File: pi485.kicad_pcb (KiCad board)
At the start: 2 copper layers, 70 x 48 mm, 29 parts, among them J1 RS485, P1 Rasperry Pi, P2 PWR, P3 Term, P4 Latch Disable, Q1 2N4401, Q2 2N4401, U1 NE555, U2 MAX485

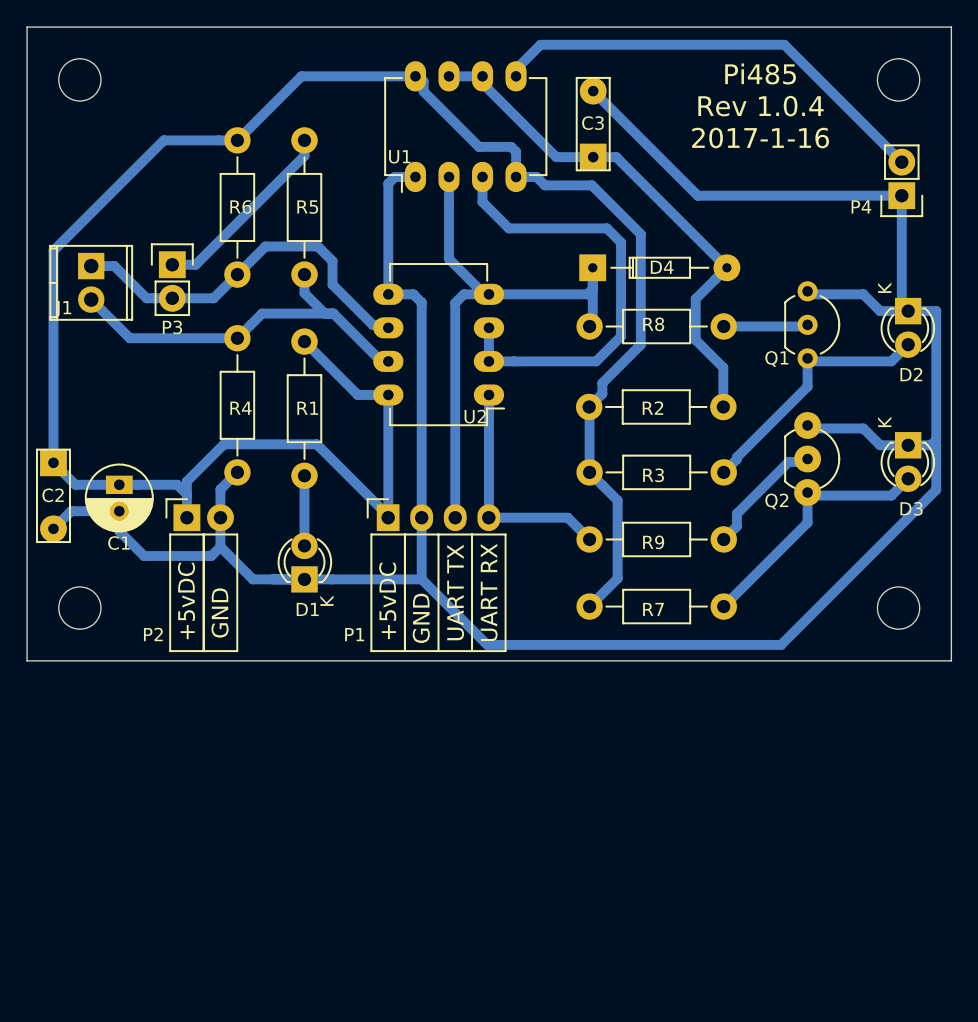
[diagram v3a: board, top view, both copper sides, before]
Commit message: 1.1.0 bump. Added 3.3v control pin to turn on power to the 485 and the PWR LED.
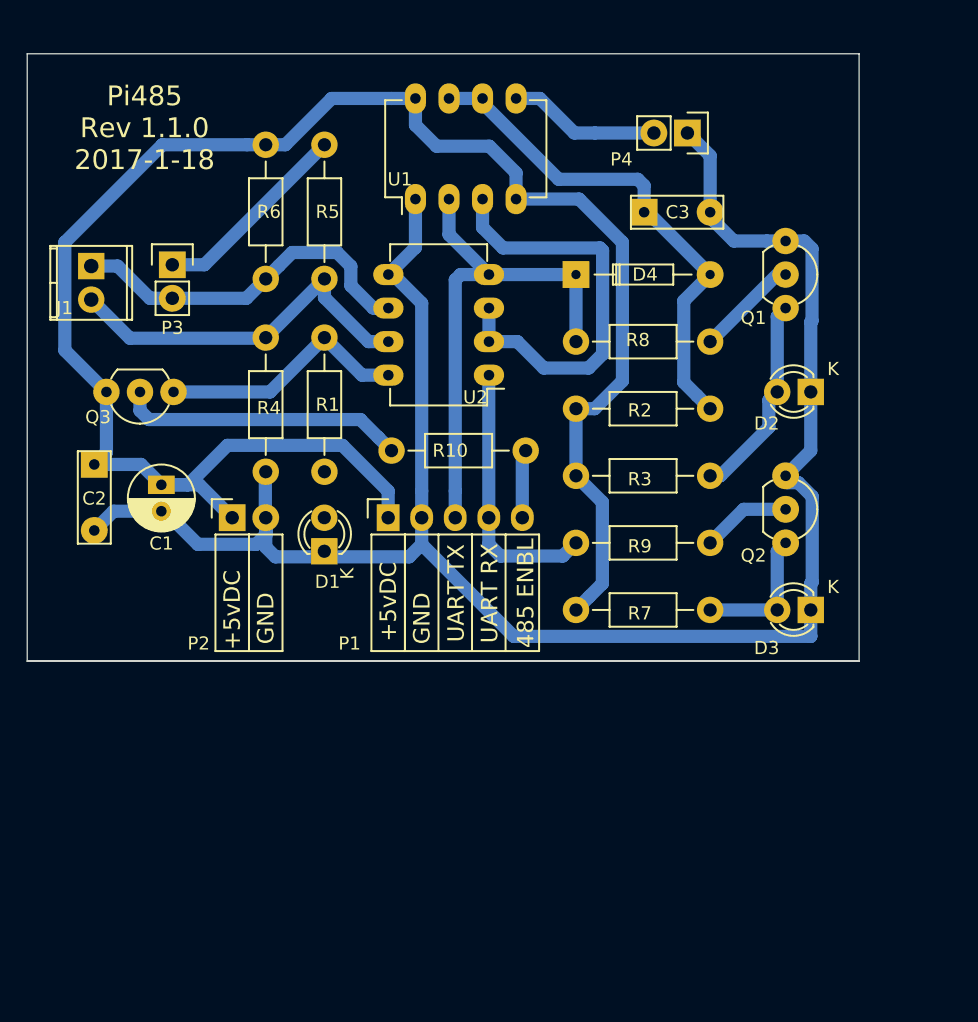
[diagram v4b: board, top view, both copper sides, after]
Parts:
- removed REF01, REF02, REF03, REF04: MountingHole_3.2mm_M3, Mounting_Holes:MountingHole_3.2mm_M3
- added Q3: 2N4401, TO_SOT_Packages_THT:TO-92_Inline_Wide, F.Cu at (23.4, 40.0)
- added R10: 270, Resistors_THT:Resistor_Horizontal_RM10mm, F.Cu at (39.9, 44.4)
- P1: footprint Socket_Strips:Socket_Strip_Angled_1x04 -> Socket_Strips:Socket_Strip_Angled_1x05
- R1: value 120 -> 200
- moved P4 16.9 mm to (62.3, 20.3), turned to 270 degrees
- moved D3 14.5 mm to (71.7, 56.5), turned to 180 degrees
- moved D2 9.59 mm to (71.7, 40.0), turned to 180 degrees
- moved C3 5.68 mm to (59.1, 26.3), turned to 0 degrees
- moved Q1 4.16 mm to (69.8, 28.5)
- moved Q2 4.16 mm to (69.8, 46.3)
- moved P2 3.43 mm to (27.9, 49.5)
- moved C1 3.19 mm to (22.5, 47.0)
- moved C2 3.09 mm to (17.4, 45.4)
- moved D1 2.61 mm to (34.8, 52.0)
- moved R6 2.17 mm to (30.4, 31.4)
- moved R4 2.15 mm to (30.4, 46.0)
- moved U1 1.68 mm to (41.7, 25.3)
- moved R5 1.55 mm to (34.9, 31.4)
- moved R1 1.54 mm to (34.9, 35.8)
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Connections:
- R1 pad 1: VCC -> Net-(Q3-Pad3)
- U2 pad 8: VCC -> Net-(Q3-Pad3)
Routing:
- net GND: track 192.4 -> 143.7 mm
- net Net-(P4-Pad2): track 34.2 -> 11.5 mm
- net Net-(Q3-Pad2): track 0.00 -> 21.7 mm
- net Net-(Q3-Pad3): track 0.00 -> 19.2 mm
- net VCC: track 154.5 -> 137.9 mm
- net Net-(D3-Pad2): track 19.2 -> 10.4 mm
- net Net-(D1-Pad2): track 5.56 -> 0.00 mm
- net /(485PWR)_GPIO18: track 0.00 -> 5.19 mm
- net /(TXDO)_GPIO14: track 43.9 -> 39.4 mm
- net Net-(D2-Pad2): track 19.2 -> 15.5 mm
- net Net-(U1-Pad3): track 35.2 -> 32.2 mm
- net Net-(Q2-Pad2): track 9.97 -> 7.13 mm
- net /(RXDO)_GPIO15: track 17.6 -> 20.2 mm
- net Net-(J1-Pad2): track 30.2 -> 28.3 mm
- net Net-(C3-Pad1): track 39.7 -> 38.5 mm
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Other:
- board size 70 x 48 mm -> 63 x 46 mm
- net class Default: clearance 0.75 -> 0.5; trace_width 0.75 -> 1
- rule trace_clearance: 0.75 -> 0.5
- rule trace_min: 0.75 -> 1
- board text added: "485 ENBL"
- board text added: "Pi485 Rev 1.1.0 2017-1-18"
- board text removed: "Pi485 Rev 1.0.4 2017-1-16"

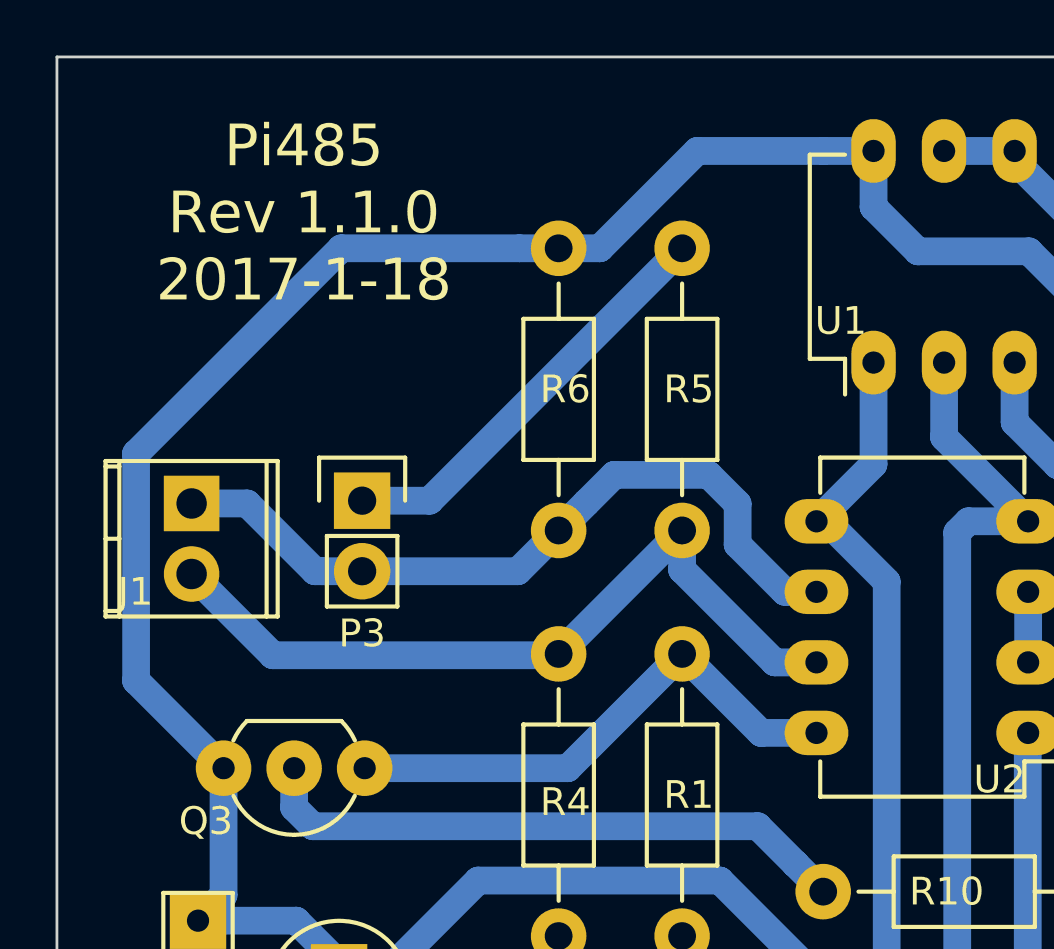
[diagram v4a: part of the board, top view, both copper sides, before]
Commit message: VCC control of the 555. Using a GPIO pin, we can reduce overall power consumption by turning things off when we don't need them.
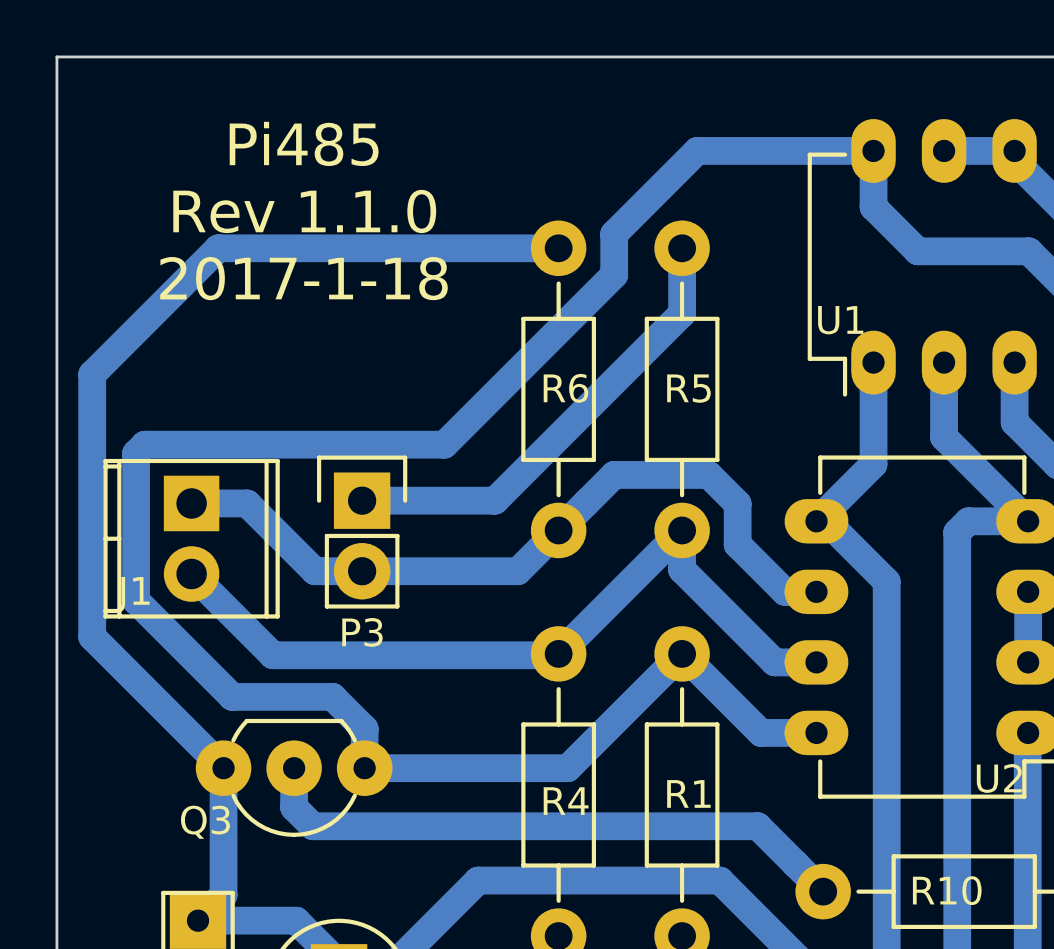
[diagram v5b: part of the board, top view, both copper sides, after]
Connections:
- R2 pad 2: VCC -> Net-(Q3-Pad3)
- U1 pad 4: VCC -> Net-(Q3-Pad3)
- U1 pad 8: VCC -> Net-(Q3-Pad3)
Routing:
- net Net-(Q3-Pad3): track 19.2 -> 110.5 mm
- net VCC: track 137.9 -> 86.5 mm
- net Net-(P3-Pad1): track 15.3 -> 16.7 mm
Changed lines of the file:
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@@
   (general
     (links 54)
-    (no_connects 0)
-    (area 12.290999 12.289999 75.391001 60.600001)
+    (no_connects 3)
+    (area 12.290999 14.289999 75.391001 60.390001)
     (thickness 1.6)
     (drawings 13)
-    (tracks 170)
+    (tracks 177)
     (zones 0)
     (modules 27)
@@
       (net 14 "Net-(C3-Pad1)"))
     (pad 2 thru_hole circle (at 10.16 0 180) (size 1.99898 1.99898) (drill 1.00076) (layers *.Cu *.SilkS *.Mask)
-      (net 7 VCC))
+      (net 17 "Net-(Q3-Pad3)"))
     (model Resistors_ThroughHole.3dshapes/Resistor_Horizontal_RM10mm.wrl
       (at (xyz 0.2 0 0))
@@
       (net 13 "Net-(U1-Pad3)"))
     (pad 4 thru_hole oval (at 0 7.62 90) (size 2.3 1.6) (drill 0.8) (layers *.Cu *.Mask)
-      (net 7 VCC))
+      (net 17 "Net-(Q3-Pad3)"))
     (pad 5 thru_hole oval (at 7.62 7.62 90) (size 2.3 1.6) (drill 0.8) (layers *.Cu *.Mask)
       (net 15 "Net-(P4-Pad2)"))
@@
       (net 14 "Net-(C3-Pad1)"))
     (pad 8 thru_hole oval (at 7.62 0 90) (size 2.3 1.6) (drill 0.8) (layers *.Cu *.Mask)
-      (net 7 VCC))
+      (net 17 "Net-(Q3-Pad3)"))
     (model Housings_DIP.3dshapes/DIP-8_W7.62mm_LongPads.wrl
       (at (xyz 0 0 0))
@@
       (effects (font (size 1 1) (thickness 0.15)))
     )
-    (fp_text value "Latch Disable" (at -3 1 540) (layer F.Fab)
+    (fp_text value "Latch Disable" (at -3 1 180) (layer F.Fab)
       (effects (font (size 1 1) (thickness 0.15)))
     )
@@
   (segment (start 44.283619 25.345) (end 44.283619 28.0332) (width 1) (layer B.Cu) (net 6))
   (segment (start 44.283619 28.0332) (end 47.310419 31.06) (width 1) (layer B.Cu) (net 6))
-  (segment (start 49.363619 25.345) (end 49.363619 23.362619) (width 1) (layer B.Cu) (net 7))
-  (segment (start 49.363619 23.362619) (end 47.341 21.34) (width 1) (layer B.Cu) (net 7))
-  (segment (start 43.341 21.34) (end 41.743619 19.742619) (width 1) (layer B.Cu) (net 7))
-  (segment (start 41.743619 19.742619) (end 41.743619 17.725) (width 1) (layer B.Cu) (net 7))
-  (segment (start 47.341 21.34) (end 43.341 21.34) (width 1) (layer B.Cu) (net 7))
-  (segment (start 30.406 21.23) (end 31.891752 21.23) (width 1) (layer B.Cu) (net 7))
-  (segment (start 31.891752 21.23) (end 35.396752 17.725) (width 1) (layer B.Cu) (net 7))
-  (segment (start 35.396752 17.725) (end 39.943619 17.725) (width 1) (layer B.Cu) (net 7))
-  (segment (start 39.943619 17.725) (end 41.743619 17.725) (width 1) (layer B.Cu) (net 7))
-  (segment (start 18.341 39.95) (end 15.190928 36.799928) (width 1) (layer B.Cu) (net 7))
-  (segment (start 15.190928 36.799928) (end 15.190928 28.618508) (width 1) (layer B.Cu) (net 7))
-  (segment (start 15.190928 28.618508) (end 22.579436 21.23) (width 1) (layer B.Cu) (net 7))
-  (segment (start 22.579436 21.23) (end 28.992508 21.23) (width 1) (layer B.Cu) (net 7))
-  (segment (start 28.992508 21.23) (end 30.406 21.23) (width 1) (layer B.Cu) (net 7))
+  (segment (start 30.406 21.23) (end 18.151 21.23) (width 1) (layer B.Cu) (net 7))
+  (segment (start 18.151 21.23) (end 13.611 25.77) (width 1) (layer B.Cu) (net 7))
+  (segment (start 13.611 35.22) (end 18.341 39.95) (width 1) (layer B.Cu) (net 7))
+  (segment (start 13.611 25.77) (end 13.611 35.22) (width 1) (layer B.Cu) (net 7))
   (segment (start 27.50449 43.995509) (end 24.517 46.982999) (width 1) (layer B.Cu) (net 7))
   (segment (start 36.213509 43.995509) (end 27.50449 43.995509) (width 1) (layer B.Cu) (net 7))
@@
   (segment (start 55.900491 54.460509) (end 54.900489 55.460511) (width 1) (layer B.Cu) (net 7))
   (segment (start 54.900489 55.460511) (end 53.901 56.46) (width 1) (layer B.Cu) (net 7))
-  (segment (start 53.901 41.22) (end 53.901 46.3) (width 1) (layer B.Cu) (net 7))
-  (segment (start 49.363619 25.345) (end 54.139336 25.345) (width 1) (layer B.Cu) (net 7))
-  (segment (start 54.139336 25.345) (end 57.417011 28.622675) (width 1) (layer B.Cu) (net 7))
-  (segment (start 57.417011 28.622675) (end 57.417011 39.117481) (width 1) (layer B.Cu) (net 7))
-  (segment (start 57.417011 39.117481) (end 55.314492 41.22) (width 1) (layer B.Cu) (net 7))
-  (segment (start 55.314492 41.22) (end 53.901 41.22) (width 1) (layer B.Cu) (net 7))
   (segment (start 53.901 51.38) (end 52.901511 52.379489) (width 1) (layer B.Cu) (net 8))
   (segment (start 52.901511 52.379489) (end 48.185489 52.379489) (width 1) (layer B.Cu) (net 8))
@@
   (segment (start 21.629909 32.857999) (end 21.893579 32.857999) (width 1) (layer B.Cu) (net 10))
   (segment (start 21.893579 32.857999) (end 23.330419 32.857999) (width 1) (layer B.Cu) (net 10))
-  (segment (start 34.851 21.23) (end 25.763001 30.317999) (width 1) (layer B.Cu) (net 11))
-  (segment (start 25.763001 30.317999) (end 23.330419 30.317999) (width 1) (layer B.Cu) (net 11))
+  (segment (start 34.851 21.23) (end 34.851 23.58) (width 1) (layer B.Cu) (net 11))
+  (segment (start 34.851 23.58) (end 28.113001 30.317999) (width 1) (layer B.Cu) (net 11))
+  (segment (start 28.113001 30.317999) (end 23.330419 30.317999) (width 1) (layer B.Cu) (net 11))
   (segment (start 39.690419 36.14) (end 38.187508 36.14) (width 1) (layer B.Cu) (net 12))
   (segment (start 38.187508 36.14) (end 34.851 32.803492) (width 1) (layer B.Cu) (net 12))
@@
   (segment (start 37.576 42.04) (end 38.931511 43.395511) (width 1) (layer B.Cu) (net 16))
   (segment (start 38.931511 43.395511) (end 39.931 44.395) (width 1) (layer B.Cu) (net 16))
+  (segment (start 41.743619 17.725) (end 35.396752 17.725) (width 1) (layer B.Cu) (net 17))
+  (segment (start 35.396752 17.725) (end 32.405491 20.716261) (width 1) (layer B.Cu) (net 17))
+  (segment (start 23.421 38.535787) (end 23.421 39.95) (width 1) (layer B.Cu) (net 17))
+  (segment (start 32.405491 20.716261) (end 32.405491 22.189757) (width 1) (layer B.Cu) (net 17))
+  (segment (start 32.405491 22.189757) (end 26.29325 28.301998) (width 1) (layer B.Cu) (net 17))
+  (segment (start 26.29325 28.301998) (end 15.507438 28.301998) (width 1) (layer B.Cu) (net 17))
+  (segment (start 15.507438 28.301998) (end 15.190928 28.618508) (width 1) (layer B.Cu) (net 17))
+  (segment (start 15.190928 28.618508) (end 15.190928 33.917756) (width 1) (layer B.Cu) (net 17))
+  (segment (start 15.190928 33.917756) (end 18.656381 37.383209) (width 1) (layer B.Cu) (net 17))
+  (segment (start 18.656381 37.383209) (end 22.268422 37.383209) (width 1) (layer B.Cu) (net 17))
+  (segment (start 22.268422 37.383209) (end 23.421 38.535787) (width 1) (layer B.Cu) (net 17))
+  (segment (start 49.363619 25.345) (end 49.363619 23.362619) (width 1) (layer B.Cu) (net 17))
+  (segment (start 49.363619 23.362619) (end 47.341 21.34) (width 1) (layer B.Cu) (net 17))
+  (segment (start 43.341 21.34) (end 41.743619 19.742619) (width 1) (layer B.Cu) (net 17))
+  (segment (start 41.743619 19.742619) (end 41.743619 17.725) (width 1) (layer B.Cu) (net 17))
+  (segment (start 47.341 21.34) (end 43.341 21.34) (width 1) (layer B.Cu) (net 17))
+  (segment (start 53.901 41.22) (end 53.901 46.3) (width 1) (layer B.Cu) (net 17))
+  (segment (start 49.363619 25.345) (end 54.139336 25.345) (width 1) (layer B.Cu) (net 17))
+  (segment (start 54.139336 25.345) (end 57.417011 28.622675) (width 1) (layer B.Cu) (net 17))
+  (segment (start 57.417011 28.622675) (end 57.417011 39.117481) (width 1) (layer B.Cu) (net 17))
+  (segment (start 57.417011 39.117481) (end 55.314492 41.22) (width 1) (layer B.Cu) (net 17))
+  (segment (start 55.314492 41.22) (end 53.901 41.22) (width 1) (layer B.Cu) (net 17))
   (segment (start 34.851 35.835) (end 37.696 38.68) (width 1) (layer B.Cu) (net 17))
   (segment (start 37.696 38.68) (end 39.690419 38.68) (width 1) (layer B.Cu) (net 17))
